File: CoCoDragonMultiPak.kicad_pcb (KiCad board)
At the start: 2 copper layers, 137.7 x 171.2 mm, 58 parts, among them IC1 74LS245DWR, IC10 74LS74ADR, IC11 74LS153DR, IC12 74AHCT30D, IC13 GAL16V8, IC2 74LS367ADR, IC3 74LS367ADR, IC4 74LS367ADR, IC5 74LS367ADR, IC6 74LS367ADR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

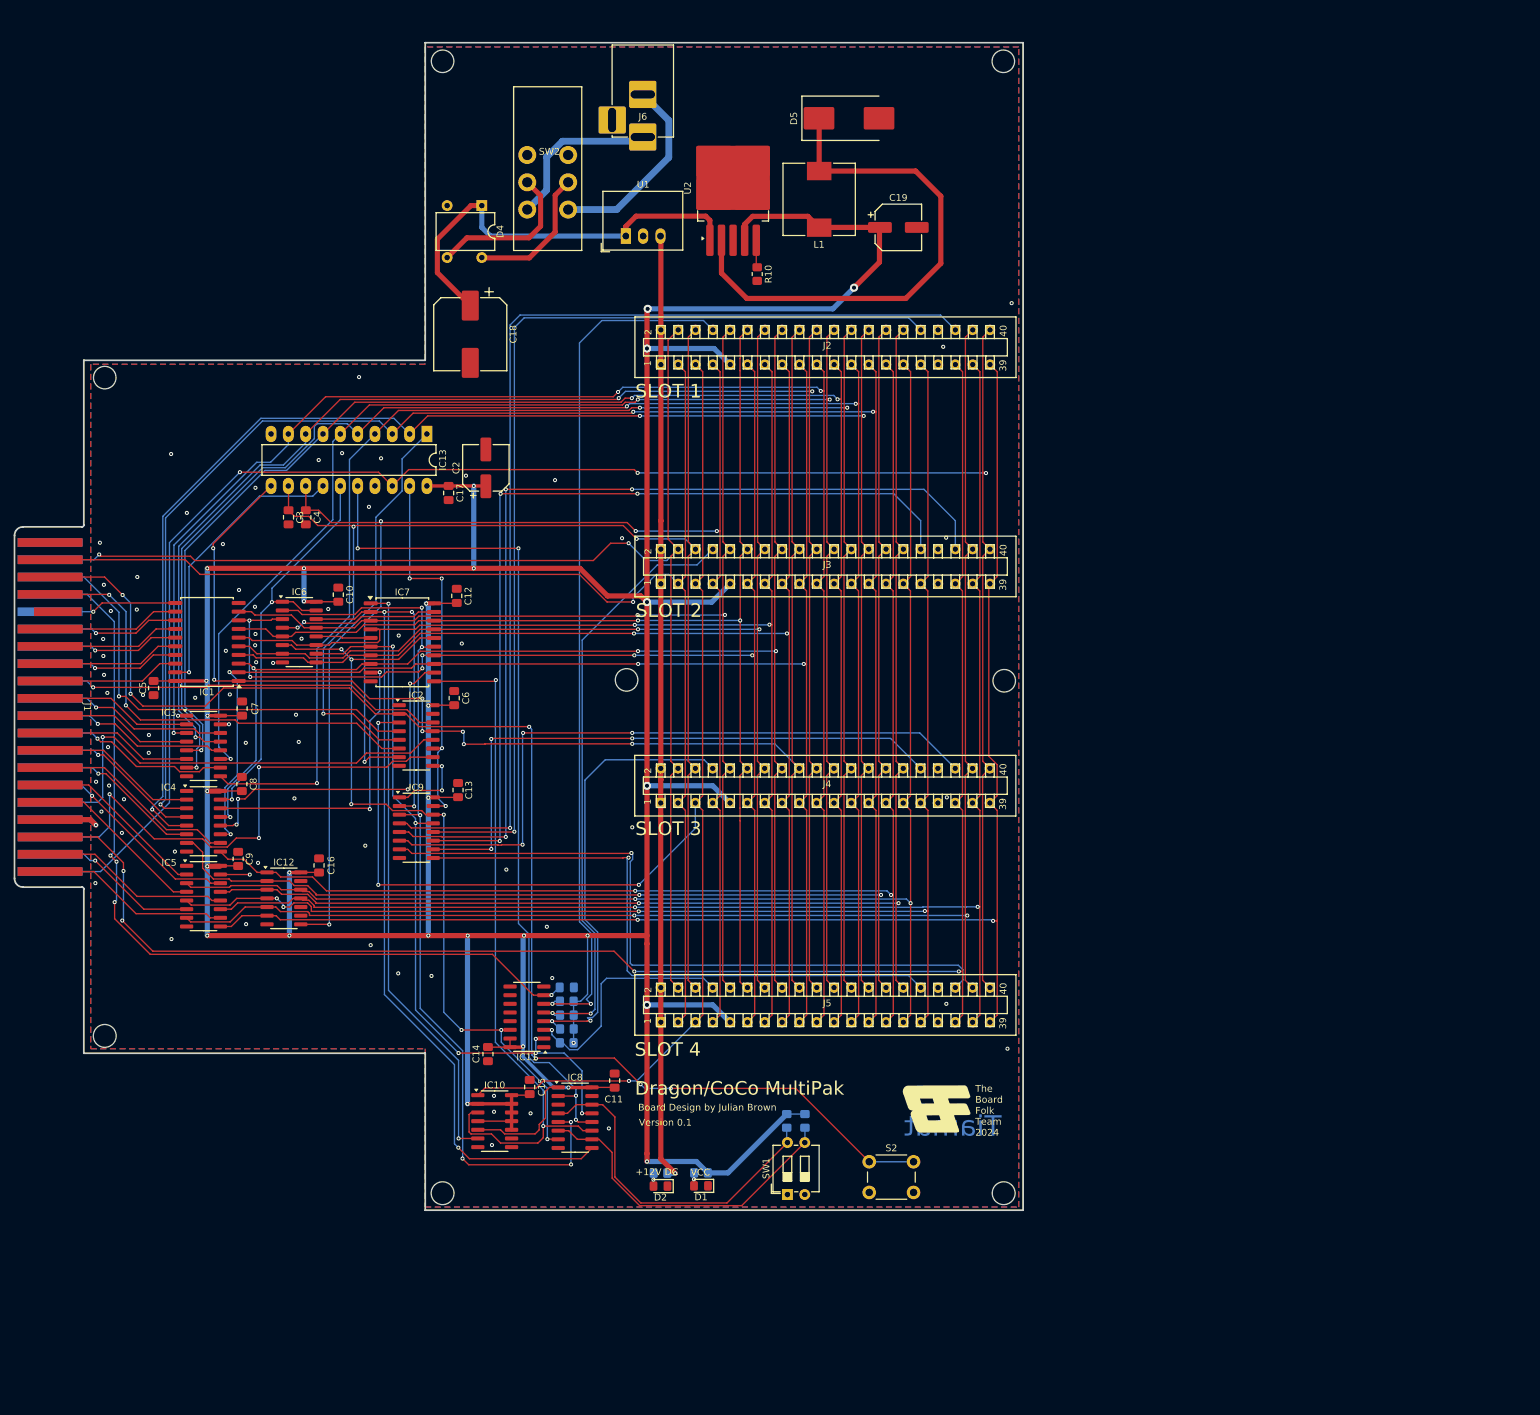
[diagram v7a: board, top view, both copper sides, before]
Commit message: switch gal for cpld
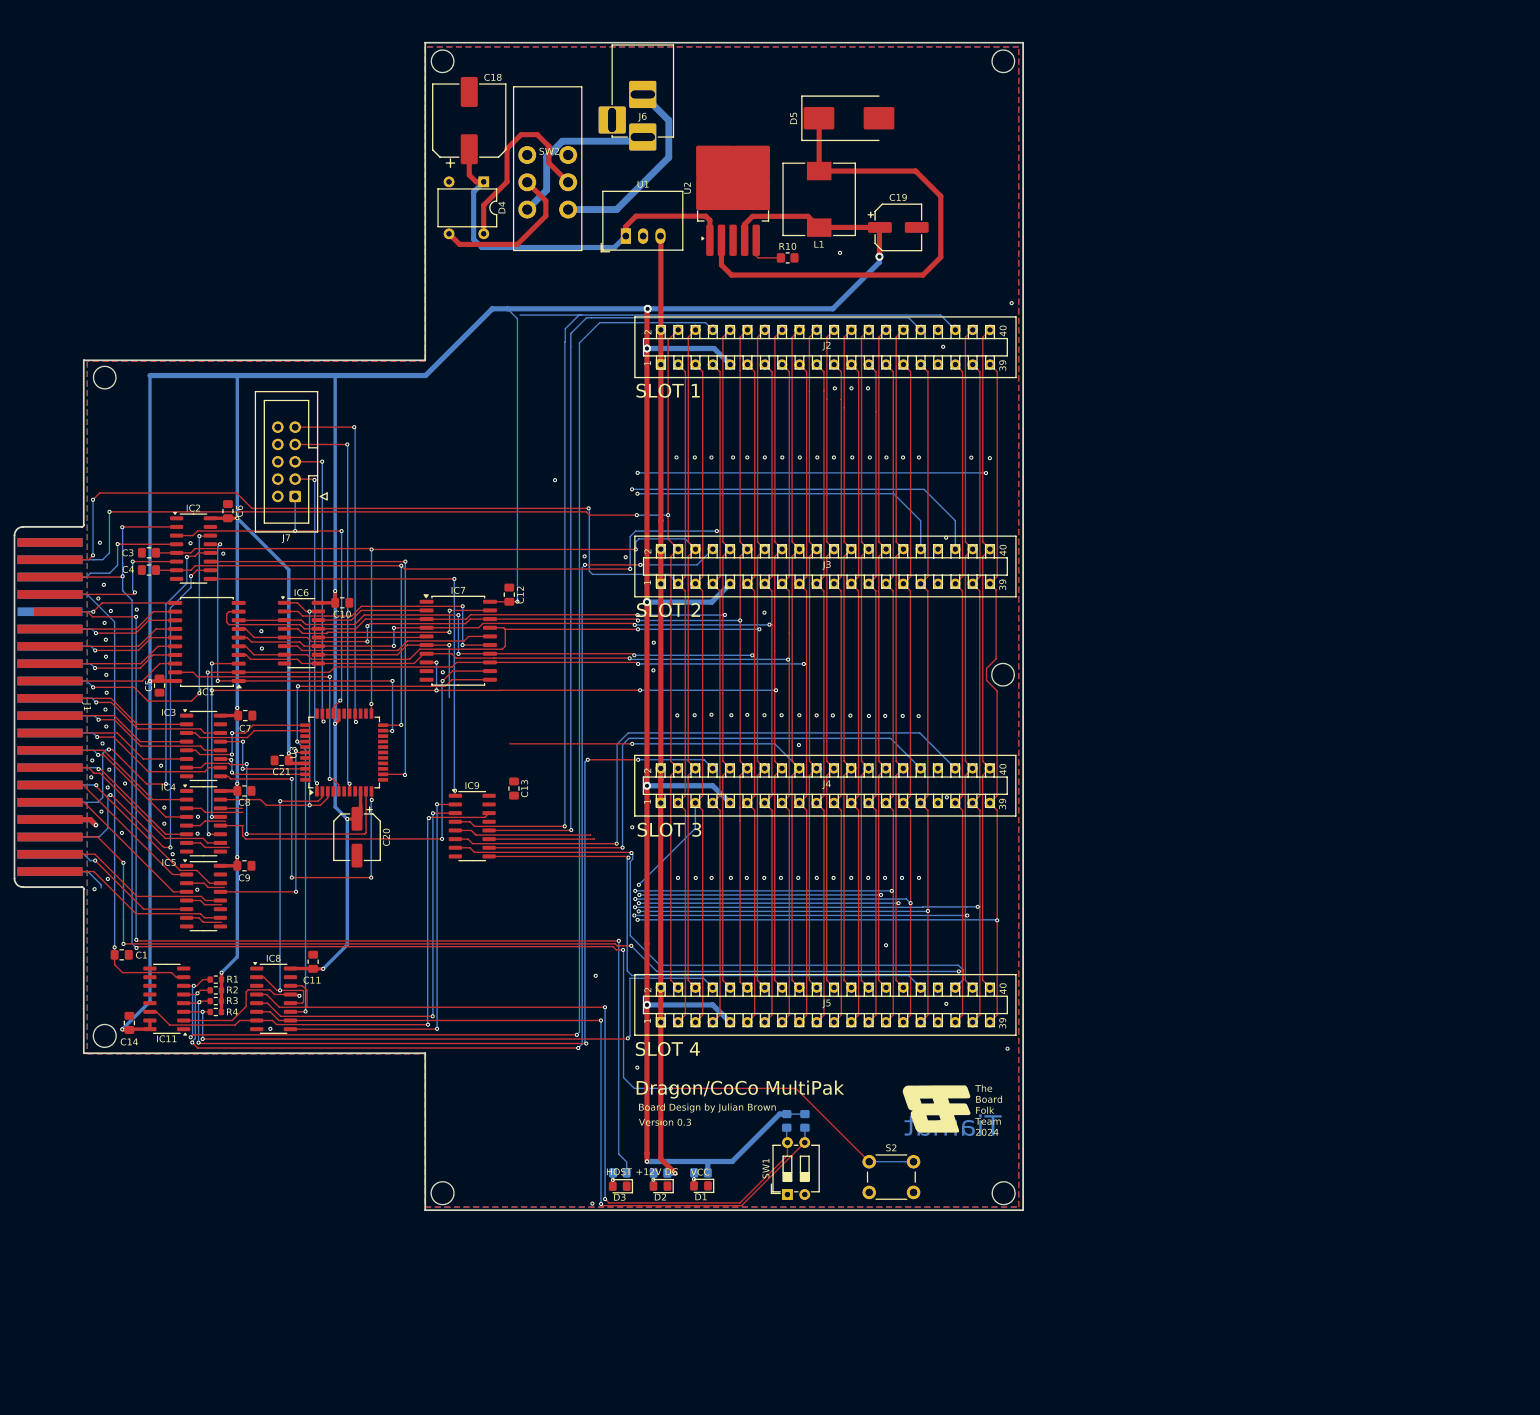
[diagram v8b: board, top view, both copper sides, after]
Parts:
- removed C15, C16, C17: 100nF, Capacitor_SMD:C_0805_2012Metric_Pad1.18x1.45mm_HandSolder
- removed C2: 220uF, Capacitor_SMD:CP_Elec_6.3x5.4_Nichicon
- removed IC10: 74LS74ADR, Package_SO:SOIC-14_3.9x8.7mm_P1.27mm
- removed IC12: 74AHCT30D, Package_SO:SOIC-14_3.9x8.7mm_P1.27mm
- removed IC13: GAL16V8, Package_DIP:DIP-20_W7.62mm_LongPads
- added C20: 220uF, Capacitor_SMD:CP_Elec_6.3x5.4_Nichicon, F.Cu at (83.7, 164.9)
- added C21: 100nF, Capacitor_SMD:C_0805_2012Metric_Pad1.18x1.45mm_HandSolder, F.Cu at (72.6, 153.7)
- added D3: LED, LED_SMD:LED_0805_2012Metric_Pad1.15x1.40mm_HandSolder, F.Cu at (122.2, 216.1)
- added J7: JTAG, Connector_IDC:IDC-Header_2x05_P2.54mm_Vertical, F.Cu at (74.6, 115.0)
- added R7: 4.7K, Resistor_SMD:R_0805_2012Metric_Pad1.20x1.40mm_HandSolder, B.Cu at (122.2, 214.1)
- added U3: ATF1504AS-xAx44, Package_QFP:TQFP-44_10x10mm_P0.8mm, F.Cu at (81.8, 152.5)
- C1: moved to F.Cu
- J1: value CARTRIDGE EDGE -> Cartridge Edge
- J2: value CARTRIDGE EDGE -> Cartridge Socket
- R1, R2, R3, R4: footprint Resistor_SMD:R_0805_2012Metric_Pad1.20x1.40mm_HandSolder -> Resistor_SMD:R_0603_1608Metric; moved to F.Cu
- moved C1 65.4 mm to (49.2, 182.2)
- moved IC11 52.9 mm to (55.8, 188.6)
- moved C14 52.8 mm to (50.3, 192.2), turned to 90 degrees
- moved R4 51.7 mm to (63.0, 190.6)
- moved R3 51.6 mm to (63.0, 189.0)
- moved R2 51.6 mm to (63.0, 187.4)
- moved R1 51.6 mm to (63.0, 185.8)
- moved IC8 47.5 mm to (71.4, 188.6)
- moved C11 47.5 mm to (77.2, 183.2)
- moved C6 43.0 mm to (64.7, 117.1)
- moved IC2 42.6 mm to (59.7, 122.6)
- moved C18 31.3 mm to (100.1, 59.9), turned to 90 degrees
- moved C4 24.3 mm to (53.2, 125.8), turned to 180 degrees
- moved C3 21.1 mm to (53.2, 123.2), turned to 180 degrees
- moved C13 8.20 mm to (106.7, 157.8)
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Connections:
- J1 pad 9: unconnected-(J1-Pin_9-Pad9) -> +5VA
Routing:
- net +5VA: track 0.00 -> 164.5 mm, vias 0 -> 3
- net /IA7: track 259.9 -> 105.1 mm, vias 3 -> 0
- net /IA6: track 257.8 -> 107.5 mm, vias 3 -> 0
- net /~{SLEN}: track 285.4 -> 159.4 mm, vias 3 -> 2
- net /IA1: track 235.5 -> 115.6 mm, vias 3 -> 2
- net /IA0: track 234.6 -> 117.2 mm, vias 3 -> 0
- net /IA2: track 237.6 -> 120.4 mm, vias 3 -> 2
- net /IA3: track 230.6 -> 113.5 mm, vias 3 -> 2
- net /IA4: track 244.3 -> 142.2 mm, vias 3 -> 2
- net /IA5: track 239.8 -> 148.5 mm, vias 3 -> 4
- net /ENREG: track 88.1 -> 0.00 mm, vias 2 -> 0
- net /FFxx: track 82.0 -> 0.00 mm, vias 1 -> 0
- net /CTRL1: track 126.4 -> 46.3 mm, vias 4 -> 2
- net +5V: track 684.6 -> 760.5 mm, vias 30 -> 20
- net /REGS0: track 149.2 -> 73.6 mm, vias 4 -> 2
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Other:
- outline, holes or cut-outs redrawn
- board text added: "HOST"
- board text added: "Version 0.3"
- board text removed: "Version 0.1"
